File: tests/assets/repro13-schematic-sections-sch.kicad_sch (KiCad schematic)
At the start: 7 parts

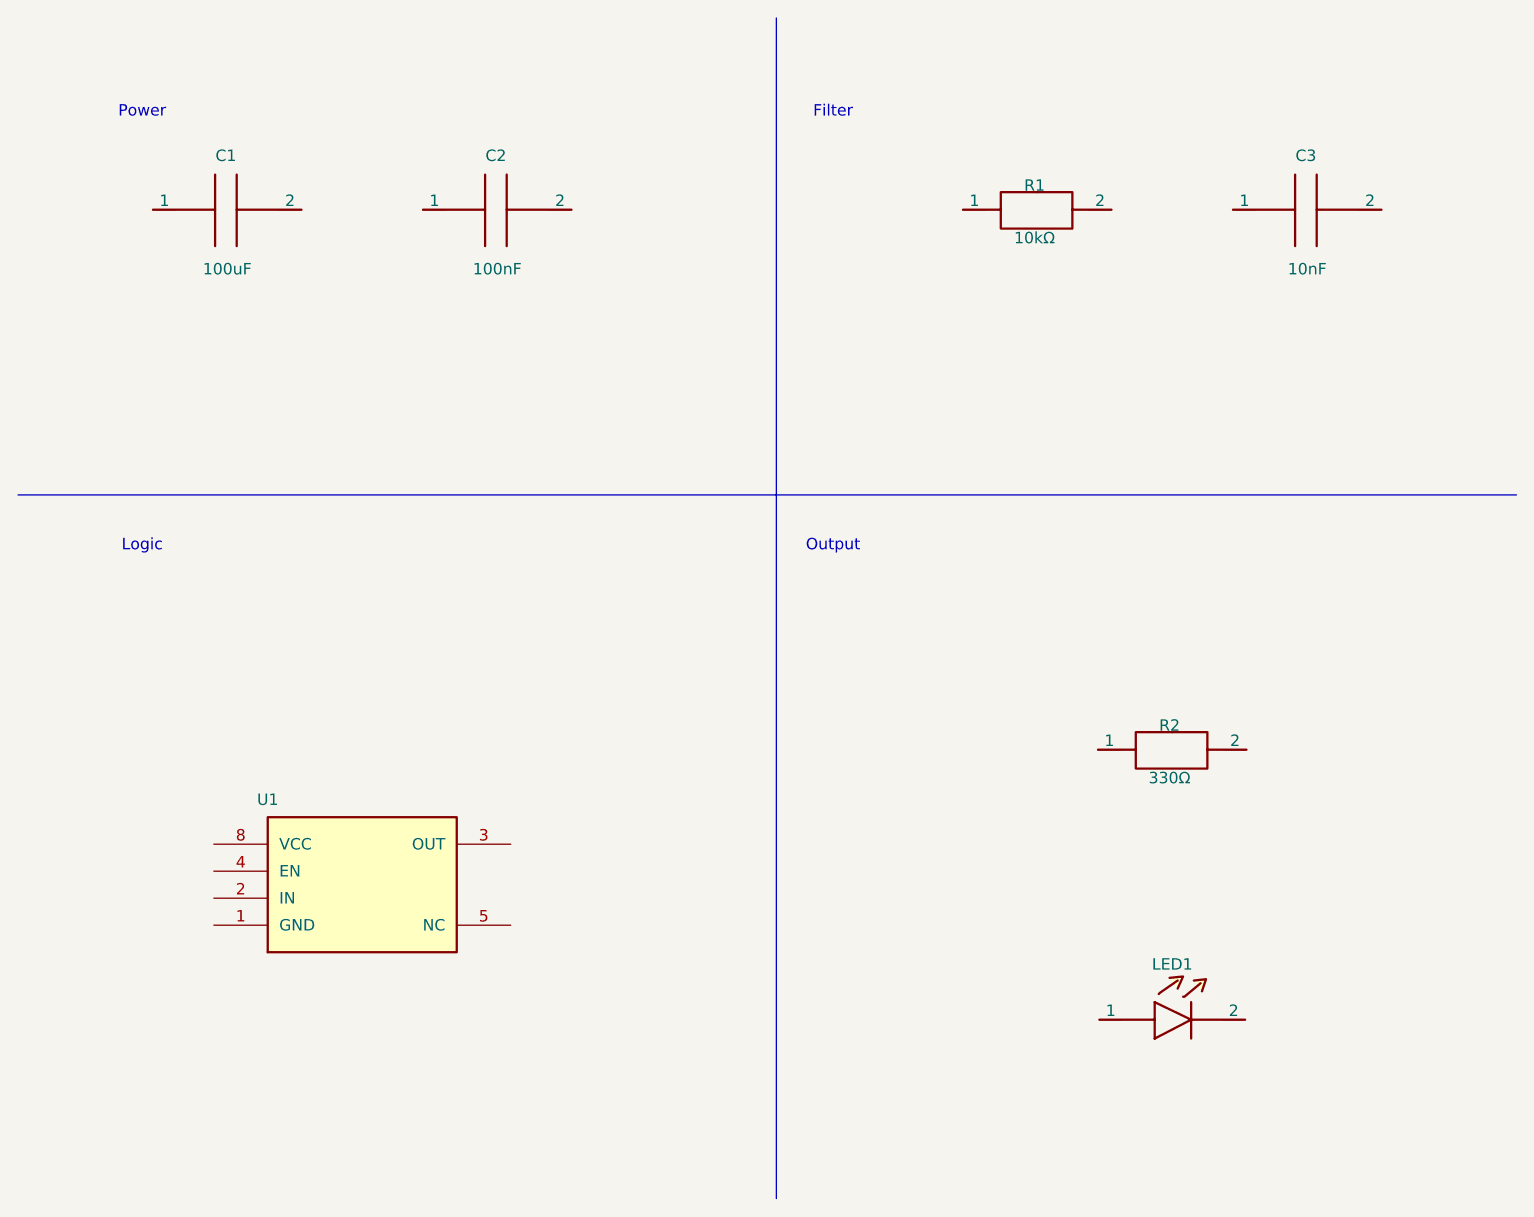
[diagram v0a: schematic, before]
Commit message: Update tscircuit to 0.0.2984 and refresh snapshots (#723)
* Update tscircuit and refresh dependency snapshots

* Refresh generated-system SVG snapshots from CI
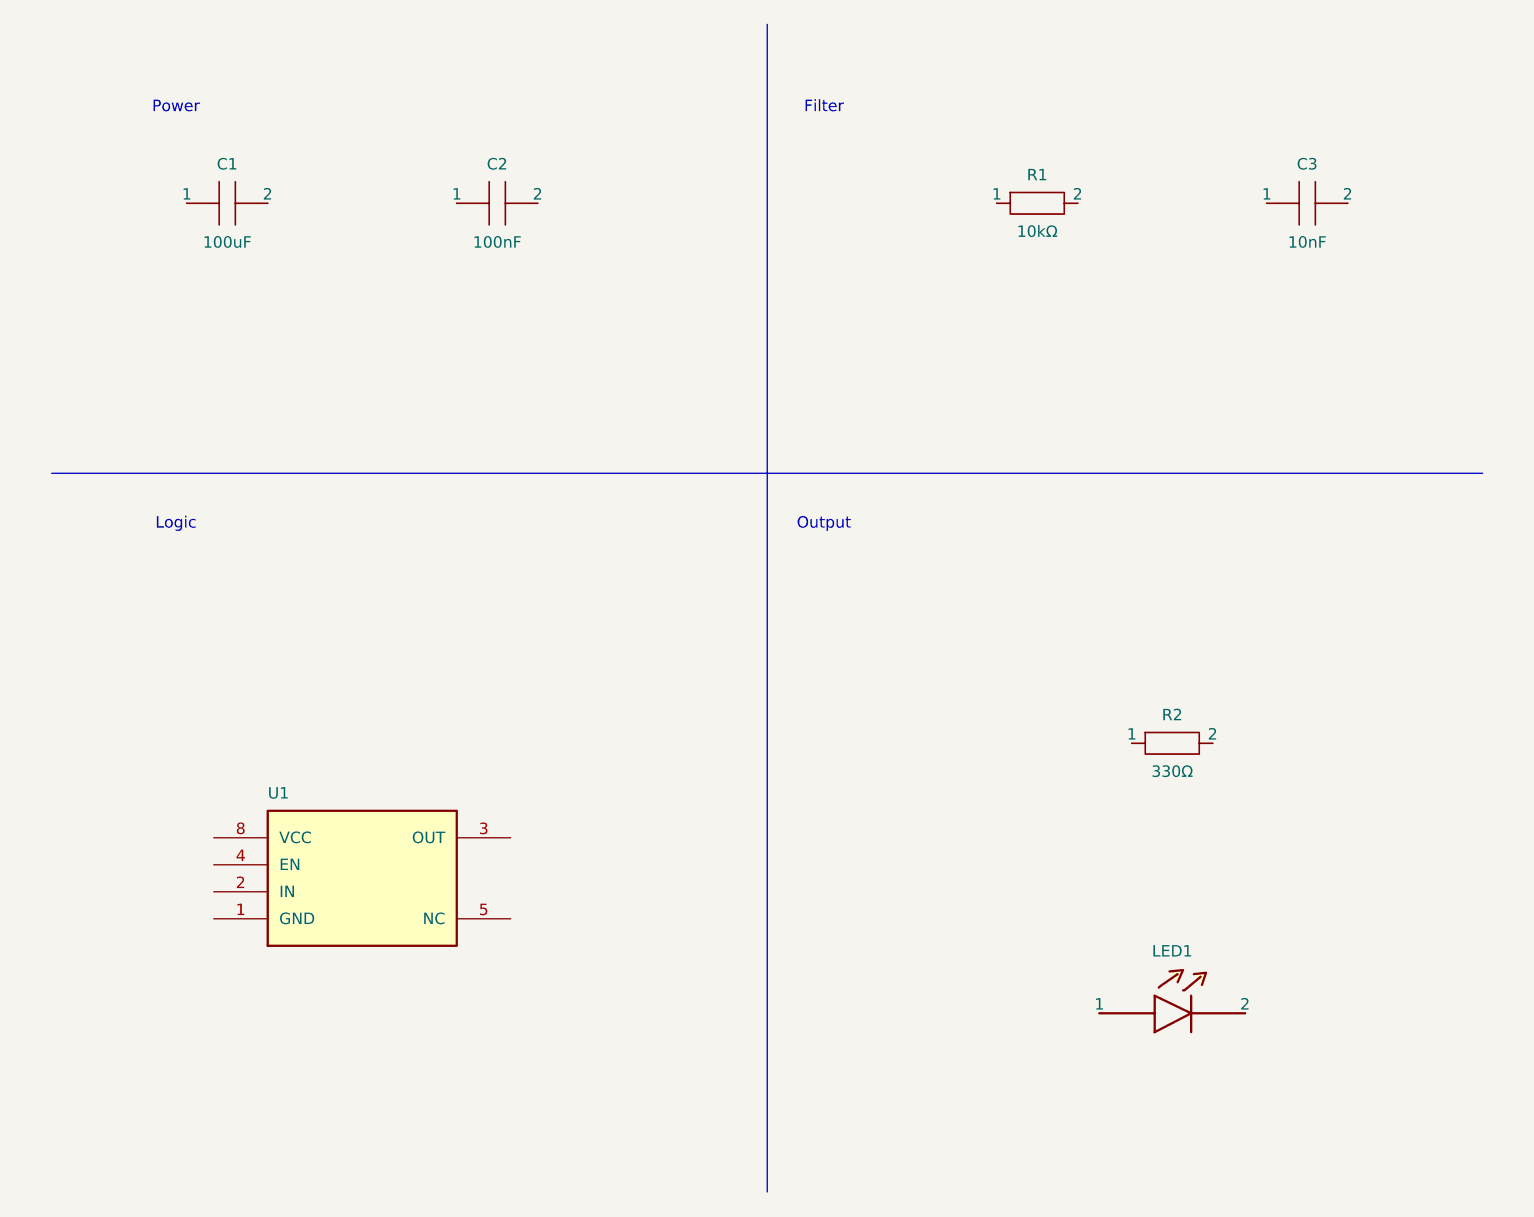
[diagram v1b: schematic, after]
